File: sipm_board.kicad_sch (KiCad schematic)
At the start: 15 parts, among them Q3 MMBT5088LT1G, Q4 MMBT5088LT1G, U10 MICROFC-60035-SMT-TR1, U9 TPS7B6950DBVR

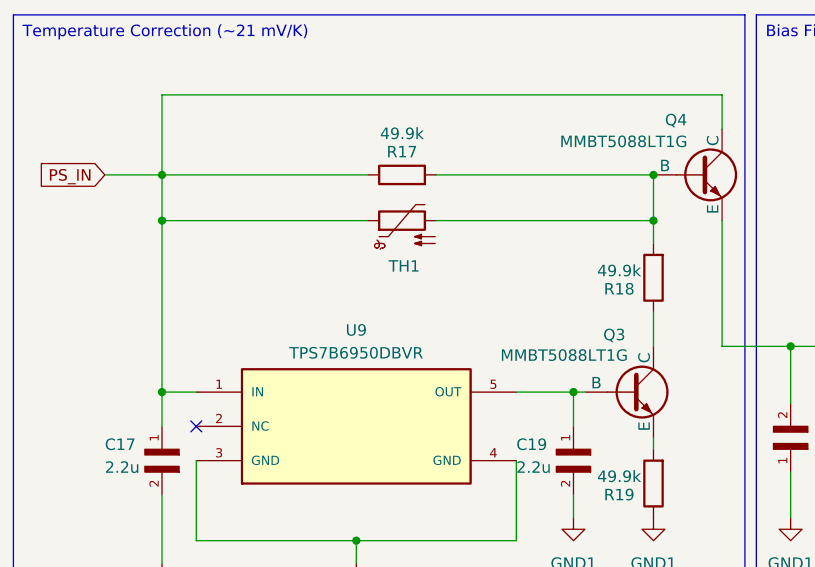
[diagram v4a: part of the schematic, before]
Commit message: Updated BOM, schematic , foortprints, symbols
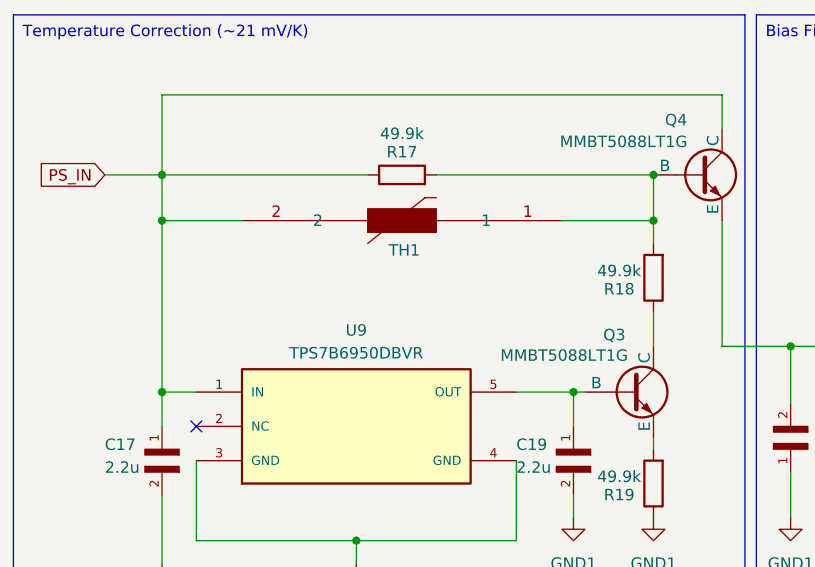
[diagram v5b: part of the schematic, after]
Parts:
- R17, R18, R19: footprint ERJ3EKF2103V:RES_ERJ3EKF2103V -> ERJ3EKF4992V:RES_ERJ3EKF4992V
- R20, R21: footprint ERJ3EKF2103V:RES_ERJ3EKF2103V -> ERJ3EKF49R9V:RES_ERJ3EKF49R9V
- TH1: footprint ERJ3EKF2103V:RES_ERJ3EKF2103V -> NTCS0603E3103FLT:NTCS0603E3103FLT; symbol Device:Thermistor_PTC -> NTCS0603E3103FLT:NTCS0603E3103FLT
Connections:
- net PS_IN: now also TH1.2; no longer TH1.1
- net at Q4.2 (B), R17.2, R18.2: now also TH1.1; no longer TH1.2
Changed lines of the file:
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@@
 		(title "SiPM Board")
 		(date "2025-01-22")
-		(rev "0.1.1")
+		(rev "0.1.2")
 		(company "Vadym Vikulin")
 		(comment 7 "Temperature Correction (~21 mV/K)")
@@
 	)
 	(junction
+		(at 154.94 73.66)
+		(diameter 0)
+		(color 0 0 0 0)
+	)
+	(junction
 		(at 154.94 68.58)
 		(diameter 0)
@@
 	)
 	(junction
-		(at 154.94 73.66)
+		(at 100.33 73.66)
 		(diameter 0)
 		(color 0 0 0 0)
@@
 	)
 	(junction
-		(at 100.33 73.66)
-		(diameter 0)
-		(color 0 0 0 0)
-	)
-	(junction
 		(at 121.92 109.22)
 		(diameter 0)
@@
 	(wire
 		(pts
+			(xy 144.78 73.66) (xy 154.94 73.66)
+		)
+		(stroke
+			(width 0)
+			(type default)
+		)
+	)
+	(wire
+		(pts
 			(xy 100.33 68.58) (xy 123.19 68.58)
 		)
@@
 	(wire
 		(pts
+			(xy 100.33 73.66) (xy 109.22 73.66)
+		)
+		(stroke
+			(width 0)
+			(type default)
+		)
+	)
+	(wire
+		(pts
 			(xy 100.33 92.71) (xy 104.14 92.71)
 		)
@@
 	(wire
 		(pts
-			(xy 130.81 73.66) (xy 154.94 73.66)
-		)
-		(stroke
-			(width 0)
-			(type default)
-		)
-	)
-	(wire
-		(pts
 			(xy 185.42 87.63) (xy 185.42 93.98)
 		)
@@
 	(wire
 		(pts
+			(xy 154.94 68.58) (xy 154.94 73.66)
+		)
+		(stroke
+			(width 0)
+			(type default)
+		)
+	)
+	(wire
+		(pts
 			(xy 154.94 73.66) (xy 154.94 76.2)
 		)
@@
 	(wire
 		(pts
-			(xy 154.94 68.58) (xy 154.94 73.66)
-		)
-		(stroke
-			(width 0)
-			(type default)
-		)
-	)
-	(wire
-		(pts
-			(xy 100.33 73.66) (xy 100.33 68.58)
-		)
-		(stroke
-			(width 0)
-			(type default)
-		)
-	)
-	(wire
-		(pts
-			(xy 100.33 73.66) (xy 123.19 73.66)
+			(xy 100.33 73.66) (xy 100.33 92.71)
 		)
 		(stroke
@@
 	(wire
 		(pts
-			(xy 100.33 92.71) (xy 100.33 73.66)
+			(xy 100.33 68.58) (xy 100.33 73.66)
 		)
 		(stroke
@@
 	)
 	(symbol
-		(lib_id "Device:Thermistor_PTC")
-		(at 127 73.66 90)
+		(lib_id "NTCS0603E3103FLT:NTCS0603E3103FLT")
+		(at 144.78 73.66 180)
 		(unit 1)
 		(exclude_from_sim no)
@@
 		(dnp no)
 		(property "Reference" "TH1"
-			(at 127.254 78.74 90)
+			(at 127.254 76.962 0)
 			(effects
 				(font
@@
 		)
 		(property "Value" "Thermistor_PTC"
-			(at 127.3175 69.85 90)
-			(effects
-				(font
-					(size 1.27 1.27)
-				)
-				(hide yes)
-			)
-		)
-		(property "Footprint" "ERJ3EKF2103V:RES_ERJ3EKF2103V"
-			(at 132.08 72.39 0)
-			(effects
-				(font
-					(size 1.27 1.27)
-				)
-				(justify left)
-				(hide yes)
-			)
-		)
-		(property "Datasheet" "~"
-			(at 127 73.66 0)
-			(effects
-				(font
-					(size 1.27 1.27)
+			(at 140.97 73.3425 90)
+			(effects
+				(font
+					(size 1.27 1.27)
+				)
+				(hide yes)
+			)
+		)
+		(property "Footprint" "NTCS0603E3103FLT:NTCS0603E3103FLT"
+			(at 144.78 73.66 0)
+			(effects
+				(font
+					(size 1.27 1.27)
+					(italic yes)
+				)
+				(hide yes)
+			)
+		)
+		(property "Datasheet" "NTCS0603E3103FLT"
+			(at 144.78 73.66 0)
+			(effects
+				(font
+					(size 1.27 1.27)
+					(italic yes)
 				)
 				(hide yes)
@@
 		)
 		(property "Description" "Temperature dependent resistor, positive temperature coefficient"
-			(at 127 73.66 0)
+			(at 144.78 73.66 0)
 			(effects
 				(font
@@
 			)
 		)
-		(property "Footprint" "ERJ3EKF2103V:RES_ERJ3EKF2103V"
+		(property "Footprint" "ERJ3EKF4992V:RES_ERJ3EKF4992V"
 			(at 156.718 80.01 90)
 			(effects
@@
 			)
 		)
-		(property "Footprint" "ERJ3EKF2103V:RES_ERJ3EKF2103V"
+		(property "Footprint" "ERJ3EKF49R9V:RES_ERJ3EKF49R9V"
 			(at 193.04 89.408 90)
 			(effects
@@
 			)
 		)
-		(property "Footprint" "ERJ3EKF2103V:RES_ERJ3EKF2103V"
+		(property "Footprint" "ERJ3EKF4992V:RES_ERJ3EKF4992V"
 			(at 156.718 102.87 90)
 			(effects
@@
 			)
 		)
-		(property "Footprint" "ERJ3EKF2103V:RES_ERJ3EKF2103V"
+		(property "Footprint" "ERJ3EKF49R9V:RES_ERJ3EKF49R9V"
 			(at 177.8 89.408 90)
 			(effects
@@
 			)
 		)
-		(property "Footprint" "ERJ3EKF2103V:RES_ERJ3EKF2103V"
+		(property "Footprint" "ERJ3EKF4992V:RES_ERJ3EKF4992V"
 			(at 127 70.358 90)
 			(effects

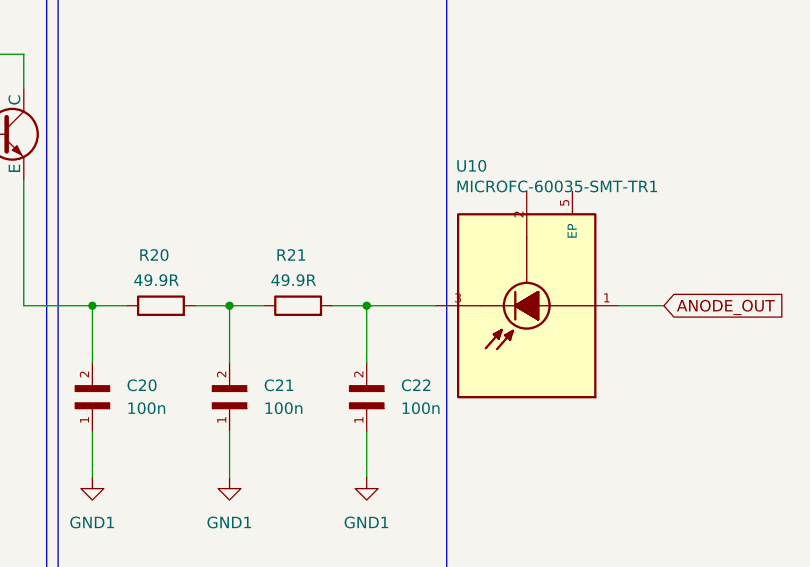
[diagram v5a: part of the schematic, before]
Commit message: Update packages for smaller size for VR1,VR2
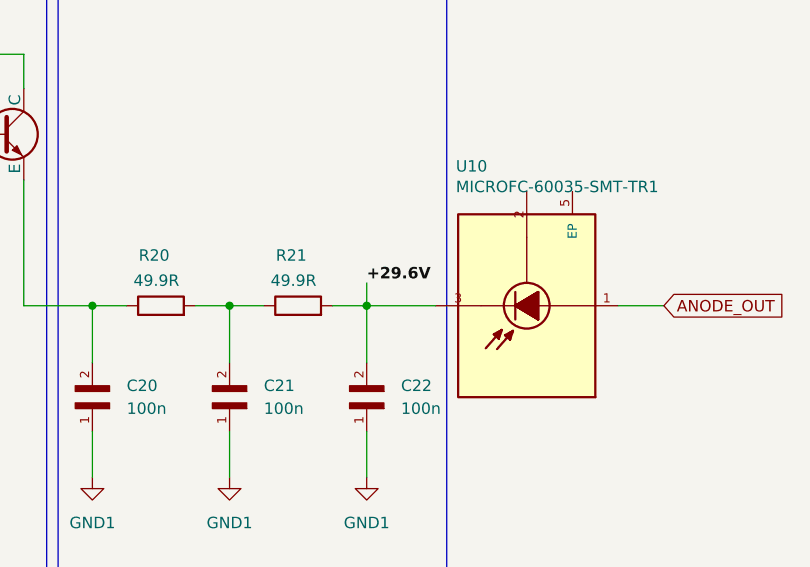
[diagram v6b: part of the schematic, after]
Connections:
- net +29.6V: now reaches C22.2, R21.2, U10.3
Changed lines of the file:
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@@
 		(title "SiPM Board")
 		(date "2025-01-22")
-		(rev "0.1.2")
+		(rev "0.1.4")
 		(company "Vadym Vikulin")
 		(comment 7 "Temperature Correction (~21 mV/K)")
@@
 		(pts
 			(xy 100.33 73.66) (xy 109.22 73.66)
+		)
+		(stroke
+			(width 0)
+			(type default)
+		)
+	)
+	(wire
+		(pts
+			(xy 200.66 85.09) (xy 200.66 87.63)
 		)
 		(stroke
@@
 		)
 	)
+	(label "+29.6V"
+		(at 200.66 85.09 0)
+		(effects
+			(font
+				(size 1.27 1.27)
+				(thickness 0.254)
+				(bold yes)
+				(color 0 0 179 1)
+			)
+			(justify left bottom)
+		)
+	)

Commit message: Updated BOM format accordingly to PCBWay format
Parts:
- Q3, Q4: MP (none) -> MMBT5088LT1G; Package (none) -> SOT95P237X111-3N
- R17, R18, R19: MP (none) -> ERJ3EKF4992V; Package (none) -> 0603
- R20, R21: MP (none) -> ERJ3EKF49R9V; Package (none) -> 0603
- TH1: MP (none) -> NTCS0603E3103FLT; Package (none) -> 0603
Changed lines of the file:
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@@
+			)
+		)
+		(property "Package" "SOT95P237X111-3N"
+			(at 152.4 92.71 0)
+			(effects
+				(font
+					(size 1.27 1.27)
+				)
+				(hide yes)
+			)
+		)
+		(property "MP" "MMBT5088LT1G"
+			(at 152.4 92.71 0)
+			(effects
+				(font
+					(size 1.27 1.27)
+				)
+				(hide yes)
 			)
 		)
@@
 			)
 		)
+		(property "MP" "NTCS0603E3103FLT"
+			(at 144.78 73.66 0)
+			(effects
+				(font
+					(size 1.27 1.27)
+				)
+				(hide yes)
+			)
+		)
+		(property "Package" "0603"
+			(at 144.78 73.66 0)
+			(effects
+				(font
+					(size 1.27 1.27)
+				)
+				(hide yes)
+			)
+		)
 		(pin "1"
 		)
@@
 			)
 		)
+		(property "Package" "SOT95P237X111-3N"
+			(at 160.02 68.58 0)
+			(effects
+				(font
+					(size 1.27 1.27)
+				)
+				(hide yes)
+			)
+		)
+		(property "MP" "MMBT5088LT1G"
+			(at 160.02 68.58 0)
+			(effects
+				(font
+					(size 1.27 1.27)
+				)
+				(hide yes)
+			)
+		)
 		(pin "2"
 		)
@@
 			)
 		)
+		(property "MP" "ERJ3EKF4992V"
+			(at 154.94 80.01 0)
+			(effects
+				(font
+					(size 1.27 1.27)
+				)
+				(hide yes)
+			)
+		)
+		(property "Package" "0603"
+			(at 154.94 80.01 0)
+			(effects
+				(font
+					(size 1.27 1.27)
+				)
+				(hide yes)
+			)
+		)
 		(pin "2"
 		)
@@
 			)
 		)
+		(property "MP" "ERJ3EKF49R9V"
+			(at 193.04 87.63 0)
+			(effects
+				(font
+					(size 1.27 1.27)
+				)
+				(hide yes)
+			)
+		)
+		(property "Package" "0603"
+			(at 193.04 87.63 0)
+			(effects
+				(font
+					(size 1.27 1.27)
+				)
+				(hide yes)
+			)
+		)
 		(pin "2"
 		)
@@
 			)
 		)
+		(property "MP" "ERJ3EKF4992V"
+			(at 154.94 102.87 0)
+			(effects
+				(font
+					(size 1.27 1.27)
+				)
+				(hide yes)
+			)
+		)
+		(property "Package" "0603"
+			(at 154.94 102.87 0)
+			(effects
+				(font
+					(size 1.27 1.27)
+				)
+				(hide yes)
+			)
+		)
 		(pin "2"
 		)
@@
 		)
 		(property "Description" "Resistor"
+			(at 177.8 87.63 0)
+			(effects
+				(font
+					(size 1.27 1.27)
+				)
+				(hide yes)
+			)
+		)
+		(property "MP" "ERJ3EKF49R9V"
+			(at 177.8 87.63 0)
+			(effects
+				(font
+					(size 1.27 1.27)
+				)
+				(hide yes)
+			)
+		)
+		(property "Package" "0603"
 			(at 177.8 87.63 0)
 			(effects
@@
 			(at 127 68.58 0)
 			(effects
+				(font
+					(size 1.27 1.27)
+				)
+				(hide yes)
+			)
+		)
+		(property "MP" "ERJ3EKF4992V"
+			(at 127 68.58 0)
+			(effects
+				(font
+					(size 1.27 1.27)
+				)
+				(hide yes)
+			)
+		)
+		(property "Package" "0603"
+			(at 127 68.58 0)
+			(effects

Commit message: Corrected BOM, Automated Gerber and Docs generation for release, bump version
BOM generation is remaining manual

Corrected manufacturer part#

Update build.yml
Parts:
- C17, C19: MP CL21A475KBQNNNE -> CL10A225KB8NNNC
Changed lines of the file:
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@@
 		(title "SiPM Board")
 		(date "2025-01-22")
-		(rev "0.1.4")
+		(rev "0.1.5")
 		(company "Vadym Vikulin")
 		(comment 7 "Temperature Correction (~21 mV/K)")
@@
 			)
 		)
-		(property "MP" "CL21A475KBQNNNE"
+		(property "MP" "CL10A225KB8NNNC"
 			(at 100.33 101.6 0)
 			(effects
@@
 			)
 		)
-		(property "MP" "CL21A475KBQNNNE"
+		(property "MP" "CL10A225KB8NNNC"
 			(at 146.05 101.6 0)
 			(effects
